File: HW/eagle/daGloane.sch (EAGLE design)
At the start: 91 parts, among them IC1 MCP1252-33X50, U1 STM32F10XTXU6, X2 SPARKFUN-CONNECTORS_USB-MICROB

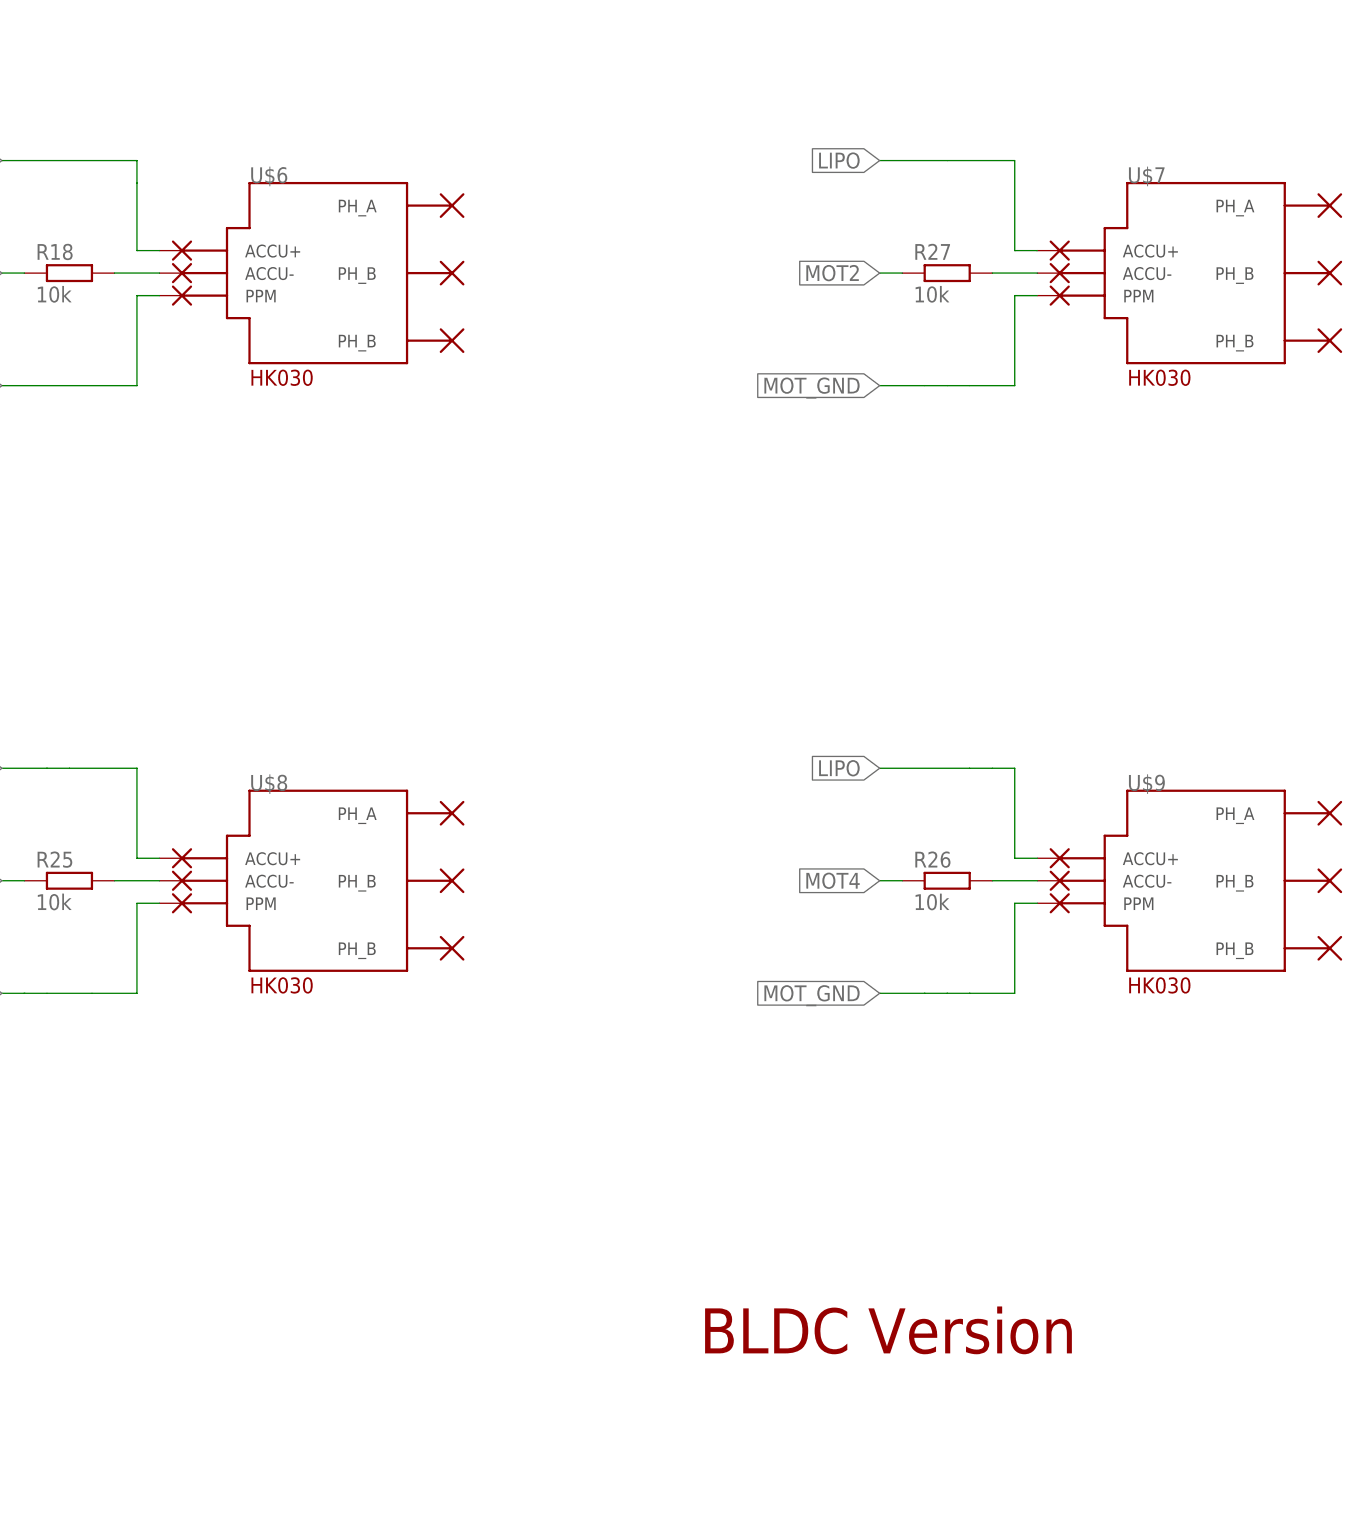
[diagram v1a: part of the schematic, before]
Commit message: testpads replaced with HK03 bldc controller symbol & package
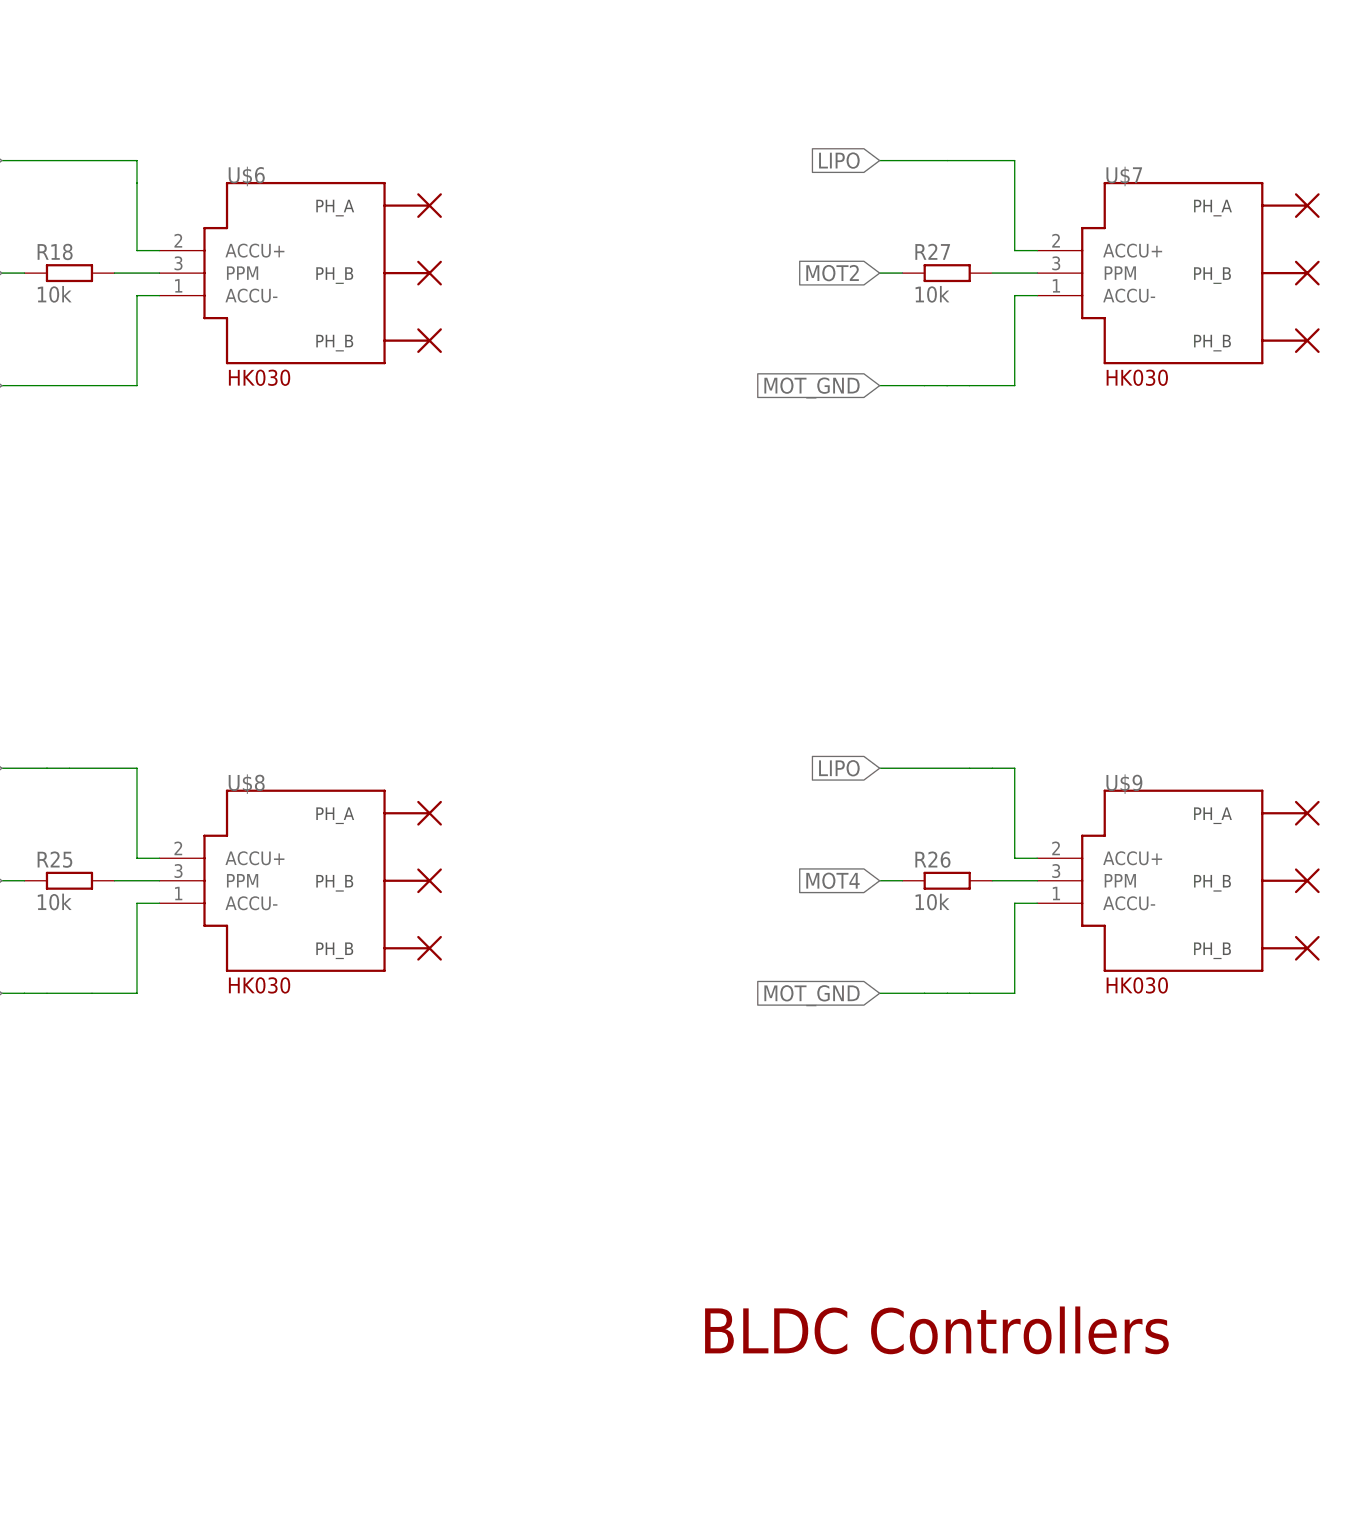
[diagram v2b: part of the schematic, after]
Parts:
- removed PAD1, PAD10, PAD11, PAD12, PAD2, PAD3, PAD4, PAD5, PAD6, PAD7, PAD8, PAD9: (no value), daGloane:SMD2
- added U$6, U$7, U$8, U$9: 3A_BLDC_CONTROLLER, daGloane:3A_BLDC_CONTROLLER
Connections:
- net LIPO: now also U$6.ACCU+, U$7.ACCU+, U$8.ACCU+, U$9.ACCU+; no longer PAD1.P, PAD10.P, PAD4.P, PAD7.P
- net MOT_GND: now also U$6.ACCU-, U$7.ACCU-, U$8.ACCU-, U$9.ACCU-; no longer PAD12.P, PAD3.P, PAD6.P, PAD9.P
- net N$22: now also U$6.PPM; no longer PAD2.P
- net N$39: now also U$7.PPM; no longer PAD11.P
- net N$40: now also U$8.PPM; no longer PAD5.P
- net N$41: now also U$9.PPM; no longer PAD8.P
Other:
- note added: "BLDC Controllers"
- note removed: "BLDC Version"
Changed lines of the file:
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@@
 <part name="U$8" library="daGloane" deviceset="3A_BLDC_CONTROLLER" device=""/>
 <part name="U$9" library="daGloane" deviceset="3A_BLDC_CONTROLLER" device=""/>
-<part name="PAD1" library="daGloane" deviceset="SMD2" device=""/>
-<part name="PAD2" library="daGloane" deviceset="SMD2" device=""/>
-<part name="PAD3" library="daGloane" deviceset="SMD2" device=""/>
-<part name="PAD4" library="daGloane" deviceset="SMD2" device=""/>
-<part name="PAD5" library="daGloane" deviceset="SMD2" device=""/>
-<part name="PAD6" library="daGloane" deviceset="SMD2" device=""/>
-<part name="PAD7" library="daGloane" deviceset="SMD2" device=""/>
-<part name="PAD8" library="daGloane" deviceset="SMD2" device=""/>
-<part name="PAD9" library="daGloane" deviceset="SMD2" device=""/>
-<part name="PAD10" library="daGloane" deviceset="SMD2" device=""/>
-<part name="PAD11" library="daGloane" deviceset="SMD2" device=""/>
-<part name="PAD12" library="daGloane" deviceset="SMD2" device=""/>
 <part name="R28" library="rcl" deviceset="R-EU_" device="R0603" value="10k"/>
 <part name="3.3V7" library="supply1" deviceset="VCC" device="" value="3.3V"/>
@@
 <text x="88.9" y="-236.22" size="5.08" layer="91">Todo:</text>
 <text x="109.22" y="-233.68" size="2.54" layer="91">easiest way to configure Module?</text>
-<text x="444.5" y="-175.26" size="5.08" layer="94">BLDC Version</text>
+<text x="444.5" y="-175.26" size="5.08" layer="94">BLDC Controllers</text>
 </plain>
 <instances>
@@
 <instance part="R26" gate="G$1" x="472.44" y="-121.92"/>
 <instance part="R27" gate="G$1" x="472.44" y="-53.34"/>
-<instance part="U$6" gate="G$1" x="401.32" y="-53.34"/>
-<instance part="U$7" gate="G$1" x="500.38" y="-53.34"/>
-<instance part="U$8" gate="G$1" x="401.32" y="-121.92"/>
-<instance part="U$9" gate="G$1" x="500.38" y="-121.92"/>
-<instance part="PAD1" gate="1" x="386.08" y="-50.8" smashed="yes" rot="R180">
-<attribute name="VALUE" x="387.223" y="-47.498" size="1.778" layer="96" rot="R180"/>
-</instance>
-<instance part="PAD2" gate="1" x="386.08" y="-53.34" smashed="yes" rot="R180">
-<attribute name="VALUE" x="387.223" y="-50.038" size="1.778" layer="96" rot="R180"/>
-</instance>
-<instance part="PAD3" gate="1" x="386.08" y="-55.88" smashed="yes" rot="R180">
-<attribute name="VALUE" x="387.223" y="-52.578" size="1.778" layer="96" rot="R180"/>
-</instance>
-<instance part="PAD4" gate="1" x="386.08" y="-119.38" smashed="yes" rot="R180">
-<attribute name="VALUE" x="387.223" y="-116.078" size="1.778" layer="96" rot="R180"/>
-</instance>
-<instance part="PAD5" gate="1" x="386.08" y="-121.92" smashed="yes" rot="R180">
-<attribute name="VALUE" x="387.223" y="-118.618" size="1.778" layer="96" rot="R180"/>
-</instance>
-<instance part="PAD6" gate="1" x="386.08" y="-124.46" smashed="yes" rot="R180">
-<attribute name="VALUE" x="387.223" y="-121.158" size="1.778" layer="96" rot="R180"/>
-</instance>
-<instance part="PAD7" gate="1" x="485.14" y="-119.38" smashed="yes" rot="R180">
-<attribute name="VALUE" x="486.283" y="-116.078" size="1.778" layer="96" rot="R180"/>
-</instance>
-<instance part="PAD8" gate="1" x="485.14" y="-121.92" smashed="yes" rot="R180">
-<attribute name="VALUE" x="486.283" y="-118.618" size="1.778" layer="96" rot="R180"/>
-</instance>
-<instance part="PAD9" gate="1" x="485.14" y="-124.46" smashed="yes" rot="R180">
-<attribute name="VALUE" x="486.283" y="-121.158" size="1.778" layer="96" rot="R180"/>
-</instance>
-<instance part="PAD10" gate="1" x="485.14" y="-50.8" smashed="yes" rot="R180">
-<attribute name="VALUE" x="486.283" y="-47.498" size="1.778" layer="96" rot="R180"/>
-</instance>
-<instance part="PAD11" gate="1" x="485.14" y="-53.34" smashed="yes" rot="R180">
-<attribute name="VALUE" x="486.283" y="-50.038" size="1.778" layer="96" rot="R180"/>
-</instance>
-<instance part="PAD12" gate="1" x="485.14" y="-55.88" smashed="yes" rot="R180">
-<attribute name="VALUE" x="486.283" y="-52.578" size="1.778" layer="96" rot="R180"/>
-</instance>
+<instance part="U$6" gate="G$1" x="398.78" y="-53.34"/>
+<instance part="U$7" gate="G$1" x="497.84" y="-53.34"/>
+<instance part="U$8" gate="G$1" x="398.78" y="-121.92"/>
+<instance part="U$9" gate="G$1" x="497.84" y="-121.92"/>
 <instance part="R28" gate="G$1" x="137.16" y="81.28" rot="R90"/>
 <instance part="3.3V7" gate="VCC" x="246.38" y="-233.68" rot="MR0"/>
@@
 <wire x1="381" y1="-43.18" x2="381" y2="-40.64" width="0.1524" layer="91"/>
 <wire x1="381" y1="-40.64" x2="365.76" y2="-40.64" width="0.1524" layer="91"/>
-<pinref part="PAD1" gate="1" pin="P"/>
+<pinref part="U$6" gate="G$1" pin="ACCU+"/>
 </segment>
 <segment>
@@
 <wire x1="482.6" y1="-50.8" x2="480.06" y2="-50.8" width="0.1524" layer="91"/>
 <wire x1="480.06" y1="-50.8" x2="480.06" y2="-40.64" width="0.1524" layer="91"/>
-<pinref part="PAD10" gate="1" pin="P"/>
 <wire x1="472.44" y1="-40.64" x2="480.06" y2="-40.64" width="0.1524" layer="91"/>
+<pinref part="U$7" gate="G$1" pin="ACCU+"/>
 </segment>
 <segment>
@@
 <wire x1="383.54" y1="-119.38" x2="381" y2="-119.38" width="0.1524" layer="91"/>
 <wire x1="381" y1="-119.38" x2="381" y2="-109.22" width="0.1524" layer="91"/>
-<pinref part="PAD4" gate="1" pin="P"/>
 <wire x1="373.38" y1="-109.22" x2="381" y2="-109.22" width="0.1524" layer="91"/>
+<pinref part="U$8" gate="G$1" pin="ACCU+"/>
 </segment>
 <segment>
@@
 <wire x1="482.6" y1="-119.38" x2="480.06" y2="-119.38" width="0.1524" layer="91"/>
 <wire x1="480.06" y1="-119.38" x2="480.06" y2="-109.22" width="0.1524" layer="91"/>
-<pinref part="PAD7" gate="1" pin="P"/>
 <wire x1="477.52" y1="-109.22" x2="480.06" y2="-109.22" width="0.1524" layer="91"/>
+<pinref part="U$9" gate="G$1" pin="ACCU+"/>
 </segment>
 </net>
@@
 <label x="365.76" y="-66.04" size="1.778" layer="95" rot="R180" xref="yes"/>
 <wire x1="381" y1="-55.88" x2="383.54" y2="-55.88" width="0.1524" layer="91"/>
-<pinref part="PAD3" gate="1" pin="P"/>
+<pinref part="U$6" gate="G$1" pin="ACCU-"/>
 </segment>
 <segment>
@@
 <wire x1="480.06" y1="-66.04" x2="480.06" y2="-55.88" width="0.1524" layer="91"/>
 <wire x1="480.06" y1="-55.88" x2="482.6" y2="-55.88" width="0.1524" layer="91"/>
-<pinref part="PAD12" gate="1" pin="P"/>
 <wire x1="474.98" y1="-66.04" x2="480.06" y2="-66.04" width="0.1524" layer="91"/>
+<pinref part="U$7" gate="G$1" pin="ACCU-"/>
 </segment>
 <segment>
@@
 <wire x1="381" y1="-134.62" x2="381" y2="-124.46" width="0.1524" layer="91"/>
 <wire x1="381" y1="-124.46" x2="383.54" y2="-124.46" width="0.1524" layer="91"/>
-<pinref part="PAD6" gate="1" pin="P"/>
 <wire x1="375.92" y1="-134.62" x2="381" y2="-134.62" width="0.1524" layer="91"/>
+<pinref part="U$8" gate="G$1" pin="ACCU-"/>
 </segment>
 <segment>
@@
 <wire x1="480.06" y1="-134.62" x2="480.06" y2="-124.46" width="0.1524" layer="91"/>
 <wire x1="480.06" y1="-124.46" x2="482.6" y2="-124.46" width="0.1524" layer="91"/>
-<pinref part="PAD9" gate="1" pin="P"/>
 <wire x1="474.98" y1="-134.62" x2="480.06" y2="-134.62" width="0.1524" layer="91"/>
+<pinref part="U$9" gate="G$1" pin="ACCU-"/>
 </segment>
 <segment>
@@
 <wire x1="383.54" y1="-53.34" x2="378.46" y2="-53.34" width="0.1524" layer="91"/>
 <pinref part="R18" gate="G$1" pin="2"/>
-<pinref part="PAD2" gate="1" pin="P"/>
+<pinref part="U$6" gate="G$1" pin="PPM"/>
 </segment>
 </net>
@@
 <wire x1="482.6" y1="-53.34" x2="477.52" y2="-53.34" width="0.1524" layer="91"/>
 <pinref part="R27" gate="G$1" pin="2"/>
-<pinref part="PAD11" gate="1" pin="P"/>
+<pinref part="U$7" gate="G$1" pin="PPM"/>
 </segment>
 </net>
@@
 <pinref part="R25" gate="G$1" pin="2"/>
 <wire x1="378.46" y1="-121.92" x2="383.54" y2="-121.92" width="0.1524" layer="91"/>
-<pinref part="PAD5" gate="1" pin="P"/>
+<pinref part="U$8" gate="G$1" pin="PPM"/>
 </segment>
 </net>
@@
 <pinref part="R26" gate="G$1" pin="2"/>
 <wire x1="477.52" y1="-121.92" x2="482.6" y2="-121.92" width="0.1524" layer="91"/>
-<pinref part="PAD8" gate="1" pin="P"/>
+<pinref part="U$9" gate="G$1" pin="PPM"/>
 </segment>
 </net>

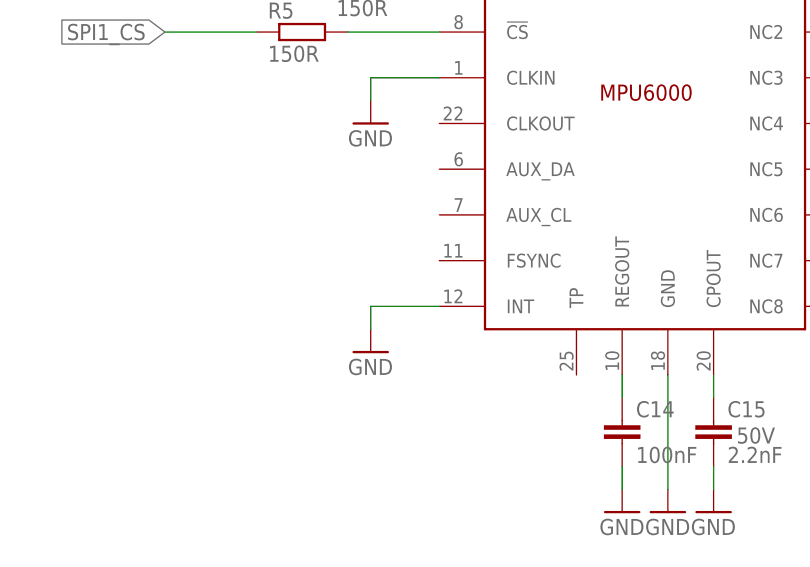
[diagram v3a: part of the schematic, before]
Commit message: error in schematic fixed: Wrong pin of MPU6000 connected to GND
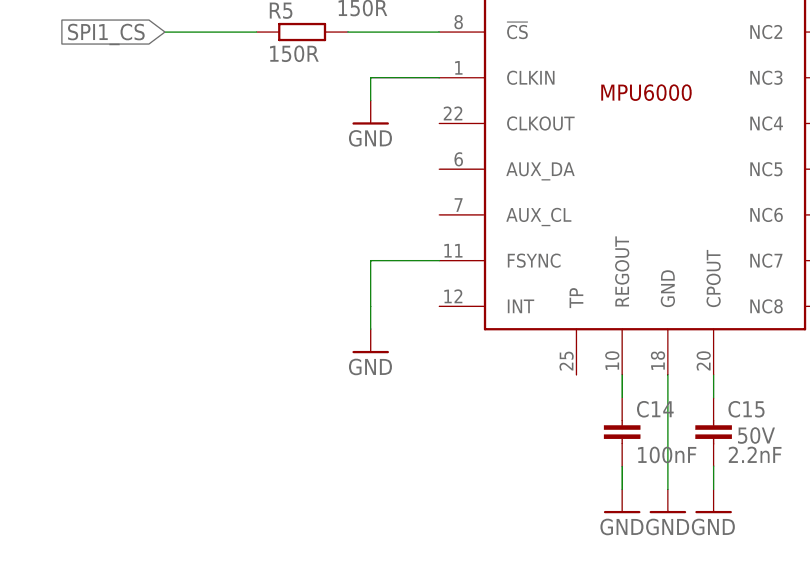
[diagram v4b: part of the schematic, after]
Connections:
- net GND: now also U$3.FSYNC; no longer U$3.INT
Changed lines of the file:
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@@
 <?xml version="1.0" encoding="utf-8"?>
 <!DOCTYPE eagle SYSTEM "eagle.dtd">
-<eagle version="6.1">
+<eagle version="6.2">
 <drawing>
 <settings>
@@
 </segment>
 <segment>
-<pinref part="U$3" gate="G$1" pin="INT"/>
 <pinref part="GND16" gate="1" pin="GND"/>
-<wire x1="284.48" y1="154.94" x2="276.86" y2="154.94" width="0.1524" layer="91"/>
 <wire x1="276.86" y1="154.94" x2="276.86" y2="152.4" width="0.1524" layer="91"/>
+<pinref part="U$3" gate="G$1" pin="FSYNC"/>
+<wire x1="284.48" y1="160.02" x2="276.86" y2="160.02" width="0.1524" layer="91"/>
+<wire x1="276.86" y1="160.02" x2="276.86" y2="154.94" width="0.1524" layer="91"/>
 </segment>
 <segment>
